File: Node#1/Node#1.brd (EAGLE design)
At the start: 100 x 80 mm, 5 parts, among them U1 BLUENRG-232

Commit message: Modified Lib, Node#1
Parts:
- added C10, C4, C5, C6, C7, C8, C9: (no value), rcl:C0805K
- added C11: (no value), rcl:C0805
- added D1: BAS40-06, diode:SOT23
- added R1, R2: (no value), rcl:R0805
- added S1: FSM4JSMAATR, BlueHome:SW_FSM4JSMAATR
- added U$2: SWITCH_L, BlueHome:R0805
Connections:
- new net N$1: C7.1, C8.1, U1.28
- new net N$2: C10.1, C9.1, U$2.2, U1.26
- new net N$3: C11.2, D1.3, R1.1, S1.3, S1.4, U1.25
- new net N$5: C11.1, R2.1, S1.1, S1.2
- new net SMPSFILT2: U$2.1, U1.27
- net +3V3: now also C4.1, C5.1, C6.1, D1.2, R1.2, U$2.3
- net 0V: now also C10.2, C4.2, C5.2, C6.2, C7.2, C8.2, C9.2, R2.2; no longer U1.28
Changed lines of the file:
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@@
 <layer number="97" name="Info" color="7" fill="1" visible="no" active="no"/>
 <layer number="98" name="Guide" color="6" fill="1" visible="no" active="no"/>
+<layer number="99" name="SpiceOrder" color="5" fill="1" visible="no" active="no"/>
 </layers>
 <board>
@@
 <element name="C3" library="rcl" package="C0805K" value="" x="-19.05" y="-10.16"/>
 <element name="U$1" library="BlueHome" package="SOT230P696X180-4N" value="BUK9840-55" x="7.62" y="6.35"/>
+<element name="C4" library="rcl" package="C0805K" value="" x="-19.05" y="-13.97"/>
+<element name="C5" library="rcl" package="C0805K" value="" x="-19.05" y="-17.78"/>
+<element name="C6" library="rcl" package="C0805K" value="" x="-19.05" y="-21.59"/>
+<element name="C7" library="rcl" package="C0805K" value="" x="-19.05" y="-25.4"/>
+<element name="C8" library="rcl" package="C0805K" value="" x="-19.05" y="-29.21"/>
+<element name="U$2" library="BlueHome" package="R0805" value="SWITCH_L" x="-17.78" y="-35.56"/>
+<element name="C9" library="rcl" package="C0805K" value="" x="-19.05" y="-41.91"/>
+<element name="C10" library="rcl" package="C0805K" value="" x="-19.05" y="-45.72"/>
+<element name="R1" library="rcl" package="R0805" value="" x="-19.05" y="-50.8"/>
+<element name="C11" library="rcl" package="C0805" value="" x="-19.05" y="-55.88"/>
+<element name="R2" library="rcl" package="R0805" value="" x="-19.05" y="-60.96"/>
+<element name="S1" library="BlueHome" package="SW_FSM4JSMAATR" value="FSM4JSMAATR" x="-13.97" y="-67.31">
+<attribute name="TE_PURCHASE_URL" value="https://www.te.com/usa-en/product-FSM4JSMAATR.html?te_bu=Cor&amp;te_type=disp&amp;te_campaign=seda_glo_cor-seda-global-disp-prtnr-fy19-seda-model-bom-cta_sma-317_1&amp;elqCampaignId=32493" x="-13.97" y="-67.31" size="1.778" layer="27" display="off"/>
+<attribute name="AVAILABILITY" value="Unavailable" x="-13.97" y="-67.31" size="1.778" layer="27" display="off"/>
+<attribute name="MF" value="TE Connectivity" x="-13.97" y="-67.31" size="1.778" layer="27" display="off"/>
+<attribute name="MP" value="FSM4JSMAATR" x="-13.97" y="-67.31" size="1.778" layer="27" display="off"/>
+<attribute name="PACKAGE" value="None" x="-13.97" y="-67.31" size="1.778" layer="27" display="off"/>
+<attribute name="DESCRIPTION" value=" Switch Tactile OFF _ON_ SPST Round Button Gull Wing 0.05A 24VDC 2.6N SMD T/R " x="-13.97" y="-67.31" size="1.778" layer="27" display="off"/>
+<attribute name="PRICE" value="None" x="-13.97" y="-67.31" size="1.778" layer="27" display="off"/>
+</element>
+<element name="D1" library="diode" package="SOT23" value="BAS40-06" x="-17.78" y="-77.47"/>
 </elements>
 <signals>
@@
 </signal>
 <signal name="+3V3">
-<contactref element="U1" pad="6"/>
-<contactref element="U1" pad="19"/>
-<contactref element="U1" pad="24"/>
 <contactref element="C1" pad="1"/>
 <contactref element="C2" pad="1"/>
+<contactref element="U1" pad="19"/>
 <contactref element="C3" pad="1"/>
+<contactref element="C4" pad="1"/>
+<contactref element="U1" pad="24"/>
+<contactref element="C5" pad="1"/>
+<contactref element="C6" pad="1"/>
+<contactref element="U1" pad="6"/>
+<contactref element="U$2" pad="3"/>
+<contactref element="R1" pad="2"/>
+<contactref element="D1" pad="2"/>
+<wire x1="-18.1" y1="-50.8" x2="-16.83" y2="-78.57" width="0" layer="19" extent="1-1"/>
+<wire x1="-15.56" y1="-35.56" x2="-18.1" y2="-50.8" width="0" layer="19" extent="1-1"/>
+<wire x1="-20.05" y1="-21.59" x2="-15.56" y2="-35.56" width="0" layer="19" extent="1-1"/>
+<wire x1="-20.05" y1="-17.78" x2="-20.05" y2="-21.59" width="0" layer="19" extent="1-1"/>
+<wire x1="-20.05" y1="-13.97" x2="-20.05" y2="-17.78" width="0" layer="19" extent="1-1"/>
+<wire x1="-20.05" y1="-10.16" x2="-20.05" y2="-13.97" width="0" layer="19" extent="1-1"/>
 <wire x1="-20.05" y1="-6.35" x2="-20.05" y2="-10.16" width="0" layer="19" extent="1-1"/>
 <wire x1="-20.05" y1="-2.54" x2="-20.05" y2="-6.35" width="0" layer="19" extent="1-1"/>
@@
 <wire x1="-15.345" y1="6.83" x2="-15.345" y2="4.33" width="0" layer="19" extent="1-1"/>
 </signal>
+<signal name="N$7">
+<contactref element="U1" pad="14"/>
+</signal>
 <signal name="0V">
-<contactref element="U1" pad="28"/>
+<contactref element="C6" pad="2"/>
+<contactref element="C5" pad="2"/>
+<contactref element="C4" pad="2"/>
+<contactref element="C3" pad="2"/>
+<contactref element="C2" pad="2"/>
 <contactref element="C1" pad="2"/>
-<contactref element="C2" pad="2"/>
-<contactref element="C3" pad="2"/>
+<contactref element="C8" pad="2"/>
+<contactref element="C7" pad="2"/>
+<contactref element="C9" pad="2"/>
+<contactref element="C10" pad="2"/>
+<contactref element="R2" pad="2"/>
+<wire x1="-18.05" y1="-45.72" x2="-18.1" y2="-60.96" width="0" layer="19" extent="1-1"/>
+<wire x1="-18.05" y1="-41.91" x2="-18.05" y2="-45.72" width="0" layer="19" extent="1-1"/>
+<wire x1="-18.05" y1="-29.21" x2="-18.05" y2="-41.91" width="0" layer="19" extent="1-1"/>
+<wire x1="-18.05" y1="-25.4" x2="-18.05" y2="-29.21" width="0" layer="19" extent="1-1"/>
+<wire x1="-18.05" y1="-21.59" x2="-18.05" y2="-25.4" width="0" layer="19" extent="1-1"/>
+<wire x1="-18.05" y1="-17.78" x2="-18.05" y2="-21.59" width="0" layer="19" extent="1-1"/>
+<wire x1="-18.05" y1="-13.97" x2="-18.05" y2="-17.78" width="0" layer="19" extent="1-1"/>
+<wire x1="-18.05" y1="-10.16" x2="-18.05" y2="-13.97" width="0" layer="19" extent="1-1"/>
 <wire x1="-18.05" y1="-6.35" x2="-18.05" y2="-10.16" width="0" layer="19" extent="1-1"/>
 <wire x1="-18.05" y1="-2.54" x2="-18.05" y2="-6.35" width="0" layer="19" extent="1-1"/>
-<wire x1="-17.53" y1="7.515" x2="-18.05" y2="-2.54" width="0" layer="19" extent="1-1"/>
-</signal>
-<signal name="N$7">
-<contactref element="U1" pad="14"/>
+</signal>
+<signal name="N$1">
+<contactref element="U1" pad="28"/>
+<contactref element="C8" pad="1"/>
+<contactref element="C7" pad="1"/>
+<wire x1="-20.05" y1="-25.4" x2="-20.05" y2="-29.21" width="0" layer="19" extent="1-1"/>
+<wire x1="-17.53" y1="7.515" x2="-20.05" y2="-25.4" width="0" layer="19" extent="1-1"/>
+</signal>
+<signal name="N$2">
+<contactref element="U1" pad="26"/>
+<contactref element="U$2" pad="2"/>
+<contactref element="C10" pad="1"/>
+<contactref element="C9" pad="1"/>
+<wire x1="-20.05" y1="-41.91" x2="-20.05" y2="-45.72" width="0" layer="19" extent="1-1"/>
+<wire x1="-17.78" y1="-35.88" x2="-20.05" y2="-41.91" width="0" layer="19" extent="1-1"/>
+<wire x1="-16.53" y1="7.515" x2="-17.78" y2="-35.88" width="0" layer="19" extent="1-1"/>
+</signal>
+<signal name="SMPSFILT2">
+<contactref element="U$2" pad="1"/>
+<contactref element="U1" pad="27"/>
+<wire x1="-17.03" y1="7.515" x2="-17.78" y2="-37.78" width="0" layer="19" extent="1-1"/>
+</signal>
+<signal name="N$3">
+<contactref element="U1" pad="25"/>
+<contactref element="R1" pad="1"/>
+<contactref element="S1" pad="3"/>
+<contactref element="S1" pad="4"/>
+<contactref element="C11" pad="2"/>
+<contactref element="D1" pad="3"/>
+<wire x1="-18.52" y1="-69.56" x2="-17.78" y2="-76.37" width="0" layer="19" extent="1-1"/>
+<wire x1="-9.42" y1="-69.56" x2="-18.52" y2="-69.56" width="0" layer="19" extent="1-1"/>
+<wire x1="-18.1" y1="-55.88" x2="-18.52" y2="-69.56" width="0" layer="19" extent="1-1"/>
+<wire x1="-20" y1="-50.8" x2="-18.1" y2="-55.88" width="0" layer="19" extent="1-1"/>
+<wire x1="-16.03" y1="7.515" x2="-20" y2="-50.8" width="0" layer="19" extent="1-1"/>
+</signal>
+<signal name="N$5">
+<contactref element="C11" pad="1"/>
+<contactref element="S1" pad="2"/>
+<contactref element="S1" pad="1"/>
+<contactref element="R2" pad="1"/>
+<wire x1="-20" y1="-60.96" x2="-18.52" y2="-65.06" width="0" layer="19" extent="1-1"/>
+<wire x1="-20" y1="-55.88" x2="-20" y2="-60.96" width="0" layer="19" extent="1-1"/>
+<wire x1="-9.42" y1="-65.06" x2="-18.52" y2="-65.06" width="0" layer="19" extent="1-1"/>
 </signal>
 </signals>

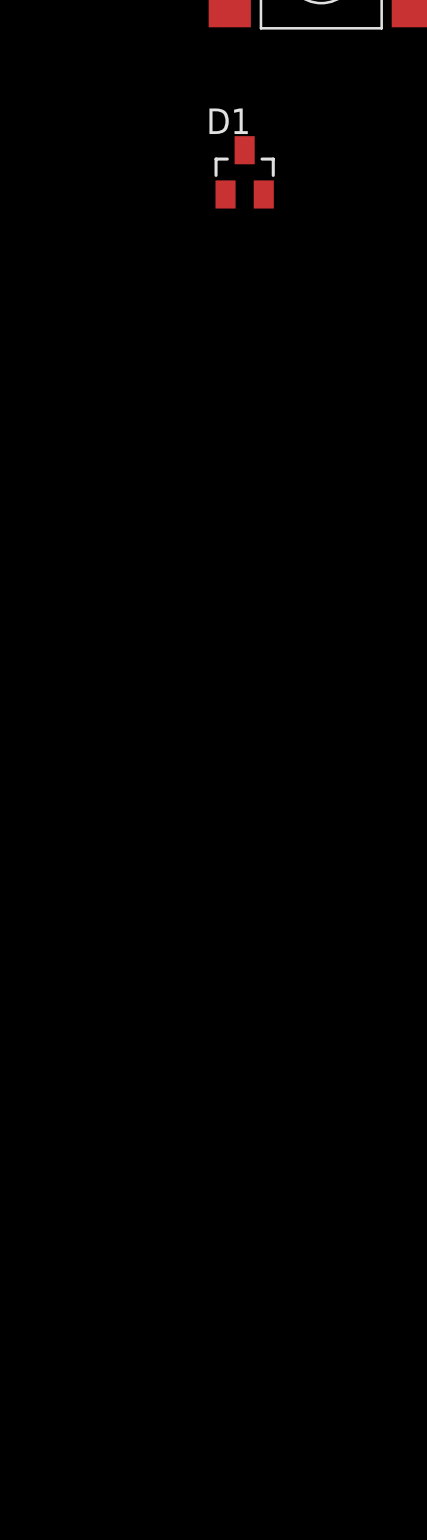
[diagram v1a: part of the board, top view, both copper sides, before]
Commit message: Modified library, Node #1 BlueNRG
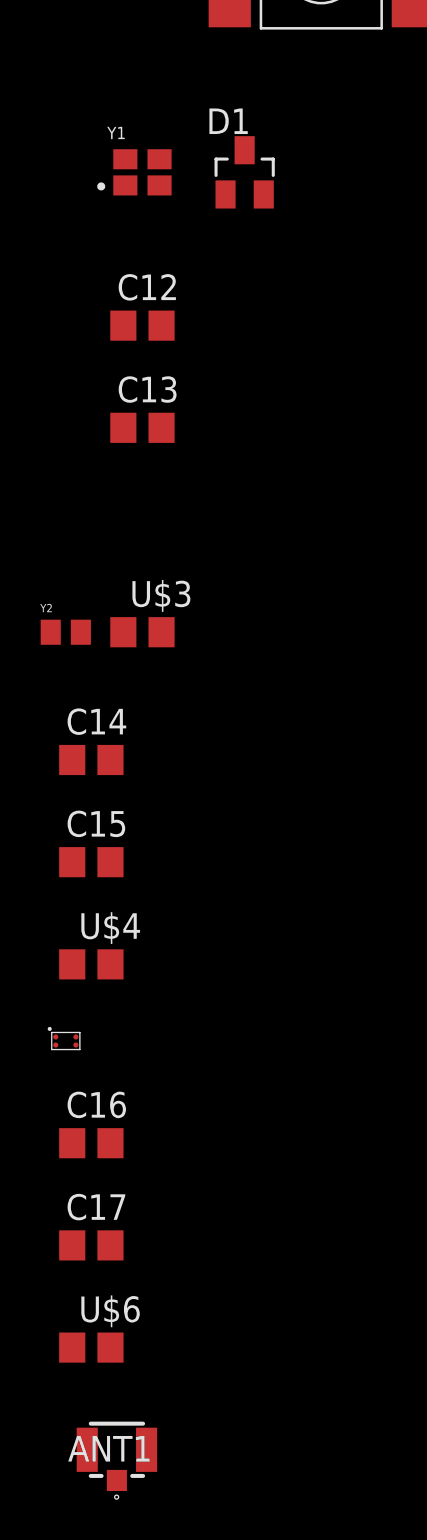
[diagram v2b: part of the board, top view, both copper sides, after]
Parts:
- added ANT1: CONUFL001-SMD, BlueHome:CONUFL001-SMD
- added C12, C13, C14, C15, C16, C17: (no value), rcl:C0805
- added U$3, U$4, U$6: L, BlueHome:R0805
- added U$5: BALF-NRG-01D3, BlueHome:FLIPCHIP
- added Y1: ECS-160-12-36-AGN-TR, BlueHome:XTAL_ECS-160-12-36-AGN-TR
- added Y2: NX2012SA-32.768K-STD-MUB-1, BlueHome:XTAL_NX2012SA-32.768K-STD-MUB-1
- U$2: device BlueHome:R0805 -> BlueHome:R0805_2
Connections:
- removed net EXP: U1.33
- new net N$10: C14.1, U1.23, Y2.2
- new net N$11: C15.1, U1.22, Y2.1
- new net N$12: U1.15
- new net N$13: U1.16
- new net N$14: U$5.B2, U1.20
- new net N$16: C16.2, U$5.A1, U$6.1
- new net N$17: ANT1.1, C17.2, U$6.2
- new net N$4: C12.1, U1.17, Y1.3
- new net N$6: C13.2, U1.18, Y1.1
- new net N$8: C13.1, U$3.1
- new net N$9: C14.2, C15.2, U$4.1
- net 0V: now also ANT1.2, ANT1.3, C12.2, C16.1, C17.1, U$3.2, U$4.2, U$5.A2, U1.31, U1.33, Y1.2, Y1.4
- net N$7: now also U$5.B1, U1.21; no longer U1.14

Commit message: Modified Node#1
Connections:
- new net RXD: U1.32
- new net SCL: U1.8
- new net SDA: U1.7
- new net TXD: U1.3
- net 0V: now also C11.1
- net N$5: no longer C11.1
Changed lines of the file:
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@@
 <contactref element="C9" pad="2"/>
 <contactref element="C10" pad="2"/>
-<contactref element="R2" pad="2"/>
 <contactref element="C12" pad="2"/>
 <contactref element="Y1" pad="4"/>
@@
 <contactref element="ANT1" pad="2"/>
 <contactref element="ANT1" pad="3"/>
+<contactref element="C11" pad="1"/>
+<contactref element="R2" pad="2"/>
 <wire x1="-22.655" y1="-140.97" x2="-25.605" y2="-140.97" width="0" layer="19" extent="1-1"/>
 <wire x1="-26.35" y1="-130.81" x2="-25.605" y2="-140.97" width="0" layer="19" extent="1-1"/>
@@
 <wire x1="-23.71" y1="-76.82" x2="-22.01" y2="-78.12" width="0" layer="19" extent="1-1"/>
 <wire x1="-18.1" y1="-60.96" x2="-23.71" y2="-76.82" width="0" layer="19" extent="1-1"/>
-<wire x1="-18.05" y1="-45.72" x2="-18.1" y2="-60.96" width="0" layer="19" extent="1-1"/>
+<wire x1="-20" y1="-55.88" x2="-18.1" y2="-60.96" width="0" layer="19" extent="1-1"/>
+<wire x1="-18.05" y1="-45.72" x2="-20" y2="-55.88" width="0" layer="19" extent="1-1"/>
 <wire x1="-18.05" y1="-41.91" x2="-18.05" y2="-45.72" width="0" layer="19" extent="1-1"/>
 <wire x1="-18.05" y1="-29.21" x2="-18.05" y2="-41.91" width="0" layer="19" extent="1-1"/>
@@
 </signal>
 <signal name="N$5">
-<contactref element="C11" pad="1"/>
 <contactref element="S1" pad="2"/>
 <contactref element="S1" pad="1"/>
 <contactref element="R2" pad="1"/>
 <wire x1="-20" y1="-60.96" x2="-18.52" y2="-65.06" width="0" layer="19" extent="1-1"/>
-<wire x1="-20" y1="-55.88" x2="-20" y2="-60.96" width="0" layer="19" extent="1-1"/>
 <wire x1="-9.42" y1="-65.06" x2="-18.52" y2="-65.06" width="0" layer="19" extent="1-1"/>
 </signal>
@@
 <wire x1="-24.45" y1="-130.81" x2="-24.45" y2="-135.89" width="0" layer="19" extent="1-1"/>
 </signal>
+<signal name="SCL">
+<contactref element="U1" pad="8"/>
+</signal>
+<signal name="SDA">
+<contactref element="U1" pad="7"/>
+</signal>
+<signal name="TXD">
+<contactref element="U1" pad="3"/>
+</signal>
+<signal name="RXD">
+<contactref element="U1" pad="32"/>
+</signal>
 </signals>

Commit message: Finished BlueNRG
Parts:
- added JP1: (no value), pinhead:2X05
- added R3, R4: (no value), rcl:R0805
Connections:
- net N$12 renamed ADC1
- net N$13 renamed ADC2
- new net DIO0: U1.12
- new net DIO1: U1.11
- new net DIO12: U1.30
- new net DIO13: U1.29
- new net DIO14: U1.13
- new net DIO2: U1.10
- new net DIO3: U1.9
- new net DIO6: U1.5
- new net DIO7: U1.4
- new net JTCK: U1.2
- new net JTMS: U1.1
- net +3V3: now also R3.2, R4.2
- net SCL: now also R3.1
- net SDA: now also R4.1
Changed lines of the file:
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@@
 <attribute name="HEIGHT" value="mm" x="-24.13" y="-140.97" size="1.778" layer="27" display="off"/>
 </element>
+<element name="R3" library="rcl" package="R0805" value="" x="-29.21" y="-147.32"/>
+<element name="R4" library="rcl" package="R0805" value="" x="-29.21" y="-152.4"/>
+<element name="JP1" library="pinhead" package="2X05" value="" x="-24.13" y="-158.75"/>
 </elements>
 <signals>
@@
 <contactref element="R1" pad="2"/>
 <contactref element="D1" pad="2"/>
+<contactref element="R4" pad="2"/>
+<contactref element="R3" pad="2"/>
+<wire x1="-28.26" y1="-147.32" x2="-28.26" y2="-152.4" width="0" layer="19" extent="1-1"/>
+<wire x1="-16.83" y1="-78.57" x2="-28.26" y2="-147.32" width="0" layer="19" extent="1-1"/>
 <wire x1="-18.1" y1="-50.8" x2="-16.83" y2="-78.57" width="0" layer="19" extent="1-1"/>
 <wire x1="-15.56" y1="-35.56" x2="-18.1" y2="-50.8" width="0" layer="19" extent="1-1"/>
@@
 <wire x1="-15.345" y1="5.83" x2="-27.42" y2="-100.33" width="0" layer="19" extent="1-1"/>
 </signal>
-<signal name="N$12">
+<signal name="ADC1">
 <contactref element="U1" pad="15"/>
 </signal>
-<signal name="N$13">
+<signal name="ADC2">
 <contactref element="U1" pad="16"/>
 </signal>
@@
 <signal name="SCL">
 <contactref element="U1" pad="8"/>
+<contactref element="R3" pad="1"/>
+<wire x1="-20.215" y1="3.33" x2="-30.16" y2="-147.32" width="0" layer="19" extent="1-1"/>
 </signal>
 <signal name="SDA">
 <contactref element="U1" pad="7"/>
+<contactref element="R4" pad="1"/>
+<wire x1="-20.215" y1="3.83" x2="-30.16" y2="-152.4" width="0" layer="19" extent="1-1"/>
 </signal>
 <signal name="TXD">
@@
 <contactref element="U1" pad="32"/>
 </signal>
+<signal name="DIO0">
+<contactref element="U1" pad="12"/>
+</signal>
+<signal name="DIO1">
+<contactref element="U1" pad="11"/>
+</signal>
+<signal name="DIO2">
+<contactref element="U1" pad="10"/>
+</signal>
+<signal name="DIO3">
+<contactref element="U1" pad="9"/>
+</signal>
+<signal name="DIO6">
+<contactref element="U1" pad="5"/>
+</signal>
+<signal name="DIO7">
+<contactref element="U1" pad="4"/>
+</signal>
+<signal name="JTCK">
+<contactref element="U1" pad="2"/>
+</signal>
+<signal name="JTMS">
+<contactref element="U1" pad="1"/>
+</signal>
+<signal name="DIO12">
+<contactref element="U1" pad="30"/>
+</signal>
+<signal name="DIO13">
+<contactref element="U1" pad="29"/>
+</signal>
+<signal name="DIO14">
+<contactref element="U1" pad="13"/>
+</signal>
 </signals>

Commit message: Finished BlueNRG 2; Added IO-Expander
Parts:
- removed U$2: SWITCH_L, BlueHome:R0805_2
- added D2, D3, D4, D5, D6, D7, D8, D9: BAS40-06, diode:SOT23
- added JMP1: 0R-JUMPA, jump-0r-smd:A0R-JMP
- added JP2: (no value), jumper:JP1
- added JP3, JP5: (no value), jumper:JP2
- added JP4: (no value), pinhead:1X03
- added LED1, LED10, LED11, LED12, LED13, LED14, LED15, LED16, LED2, LED3, LED4, LED5, LED6, LED7, LED8, LED9: (no value), led:LED3MM
- added R10, R11, R12, R13, R14, R15, R16, R17, R18, R19, R20, R21, R22, R23, R24, R25, R26, R27, R28, R29, R30, R31, R32, R33, R34, R35, R36, R37, R38, R5, R6, R7, R8, R9: (no value), rcl:R0805
- added U2: SEMTECH_SX1503I091TRTSEMTECH_SX1503I091TRT_0_0, BlueHome:SEMTECH_SX1503I091TRT_0
- added X1, X3: 2081-1228, BlueHome:P-2081-1228
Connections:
- new net +5V: JP3.3, JP5.3
- new net GND: ANT1.2, ANT1.3, C1.2, C10.2, C11.1, C16.1, C17.1, C2.2, C3.2, C4.2, C5.2, C6.2, C7.2, C8.2, C9.2, D2.3, D3.3, D4.3, D5.3, D6.3, D7.3, D8.3, D9.3, JP1.3, JP1.5, JP1.9, JP4.3, LED1.K, LED10.K, LED11.K, LED12.K, LED13.K, LED14.K, LED15.K, LED16.K, LED2.K, LED3.K, LED4.K, LED5.K, LED6.K, LED7.K, LED8.K, LED9.K, R2.2, U$4.2, U$5.A2, U1.31, U1.33, U2.1, U2.15, U2.21, U2.29, U2.7, Y1.2, Y1.4
- new net N$12: JP3.2, U2.4
- new net N$13: JP5.2, U2.18
- new net N$15: D2.1, R7.2, R8.2, U2.27
- new net N$18: R9.1, X1.L7
- new net N$19: LED9.A, R10.2
- new net N$20: D3.2, R13.2, R14.1, U2.3
- new net N$21: D4.1, R15.2, R16.2, U2.5
- new net N$22: D4.2, R17.2, R18.1, U2.6
- new net N$23: D6.2, R25.2, R26.1, U2.14
- new net N$24: R13.1, X1.L5
- new net N$25: D6.1, R23.2, R24.2, U2.13
- new net N$27: D7.1, R27.2, R28.2, U2.16
- new net N$28: D7.2, R29.2, R30.1, U2.17
- new net N$29: D8.1, R31.2, R32.2, U2.19
- new net N$30: D8.2, R33.2, R34.1, U2.20
- new net N$31: D9.1, R35.2, R36.2, U2.22
- new net N$32: D9.2, R37.2, R38.1, U2.23
- new net N$33: LED1.A, R7.1
- new net N$34: R25.1, X3.L7
- new net N$35: D2.2, R10.1, R9.2, U2.28
- new net N$36: R8.1, X1.L8
- new net N$37: D3.1, R11.2, R12.2, U2.2
- new net N$38: LED10.A, R11.1
- new net N$40: R12.1, X1.L6
- new net N$41: LED11.A, R14.2
- new net N$42: R17.1, X1.L3
- new net N$43: LED12.A, R15.1
- new net N$45: R16.1, X1.L4
- new net N$46: LED13.A, R18.2
- new net N$47: D5.1, R19.2, R20.2, U2.8
- new net N$48: R21.1, X1.L1
- new net N$49: LED14.A, R19.1
- new net N$50: D5.2, R21.2, R22.1, U2.9
- new net N$51: R20.1, X1.L2
- new net N$52: LED15.A, R22.2
- new net N$54: LED2.A, R23.1
- new net N$56: R24.1, X3.L8
- new net N$58: LED3.A, R26.2
- new net N$59: R29.1, X3.L5
- new net N$60: LED4.A, R27.1
- new net N$61: R28.1, X3.L6
- new net N$62: LED5.A, R30.2
- new net N$63: R33.1, X3.L3
- new net N$64: LED6.A, R31.1
- new net N$65: R32.1, X3.L4
- new net N$66: LED7.A, R34.2
- new net N$68: R37.1, X3.L1
- new net N$69: LED8.A, R35.1
- new net N$71: R36.1, X3.L2
- new net N$72: LED16.A, R38.2
- new net RESETN: C11.2, D1.3, JP1.10, R1.1, S1.3, S1.4, U1.25, U2.24
- new net TDI: JP1.8, R5.1, U1.12
- new net TDO: JP1.6, R6.1, U1.11
- net +3V3: now also JMP1.3, JP2.2, JP3.1, JP5.1, U2.12; no longer U$2.3
- net 0V: no longer ANT1.2, ANT1.3, C1.2, C10.2, C11.1, C16.1, C17.1, C2.2, C3.2, C4.2, C5.2, C6.2, C7.2, C8.2, C9.2, R2.2, U$4.2, U$5.A2, U1.31, U1.33, Y1.2, Y1.4
- net DIO0: now also R5.2; no longer U1.12
- net DIO1: now also R6.2; no longer U1.11
- net JTCK: now also JP1.4
- net JTMS: now also JP1.2
- net N$2: now also JMP1.2; no longer U$2.2
- net N$3: now also JP1.1, JP2.1; no longer C11.2, D1.3, R1.1, S1.3, S1.4, U1.25
- net RXD: now also JP4.2
- net SCL: now also U2.26
- net SDA: now also U2.25
- net SMPSFILT2: now also JMP1.1; no longer U$2.1
- net TXD: now also JP4.1

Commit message: Output Driver Node#1
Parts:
- added JP7: (no value), pinhead:1X08
- added R39, R40, R41, R42: (no value), rcl:R1210
- added U$2, U$7, U$8: BUK9840-55, BlueHome:SOT230P696X180-4N
- added U3: MIC4468YWM, BlueHome:SOIC127P1030X265-16N
- added U4: LM339ADR, BlueHome:SOIC127P600X175-14N
- added X2: 2081-1228, BlueHome:P-2081-1228
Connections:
- new net N$26: R24.1, X1.L4
- new net N$39: U3.8
- new net N$44: U3.2, U3.4, U3.6, U3.9
- new net N$53: R39.1, U3.13
- new net N$55: U3.1
- new net N$57: U3.5
- new net N$67: R40.1, U3.12
- new net N$70: R41.1, U3.11
- new net N$73: R42.1, U3.10
- new net N$74: R39.2, U$1.1
- new net N$75: R40.2, U$2.1
- new net N$76: R41.2, U$7.1
- new net N$77: R42.2, U$8.1
- new net N$78: U$1.2, X3.L7
- new net N$79: U$8.2, X3.L1
- new net N$80: U$7.2, X3.L3
- new net N$81: U$2.2, X3.L5
- new net N$83: X3.L2, X3.L4, X3.L6, X3.L8
- new net VCC: U4.3
- net GND: now also U$1.3, U$2.3, U$7.3, U$8.3, U3.7
- net N$34: now also X1.L3; no longer X3.L7
- net N$42: now also JP7.2; no longer X1.L3
- net N$45: now also JP7.1; no longer X1.L4
- net N$48: now also JP7.4; no longer X1.L1
- net N$51: now also JP7.3; no longer X1.L2
- net N$56: now also U3.3; no longer R24.1, X3.L8
- net N$59: now also X1.L1; no longer X3.L5
- net N$61: now also X1.L2; no longer X3.L6
- net N$63: now also JP7.6; no longer X3.L3
- net N$65: now also JP7.5; no longer X3.L4
- net N$68: now also JP7.8; no longer X3.L1
- net N$71: now also JP7.7; no longer X3.L2
